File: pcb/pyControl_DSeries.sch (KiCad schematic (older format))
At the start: 14 parts, among them J1 Barrel_Jack, J2 RJ45-12PORT, U1 PyBoard-D-Series, U2 R-78E5.0-1.0, U3 TBD62083APG, U4 TBD62083APG, U5 TBD62083APG

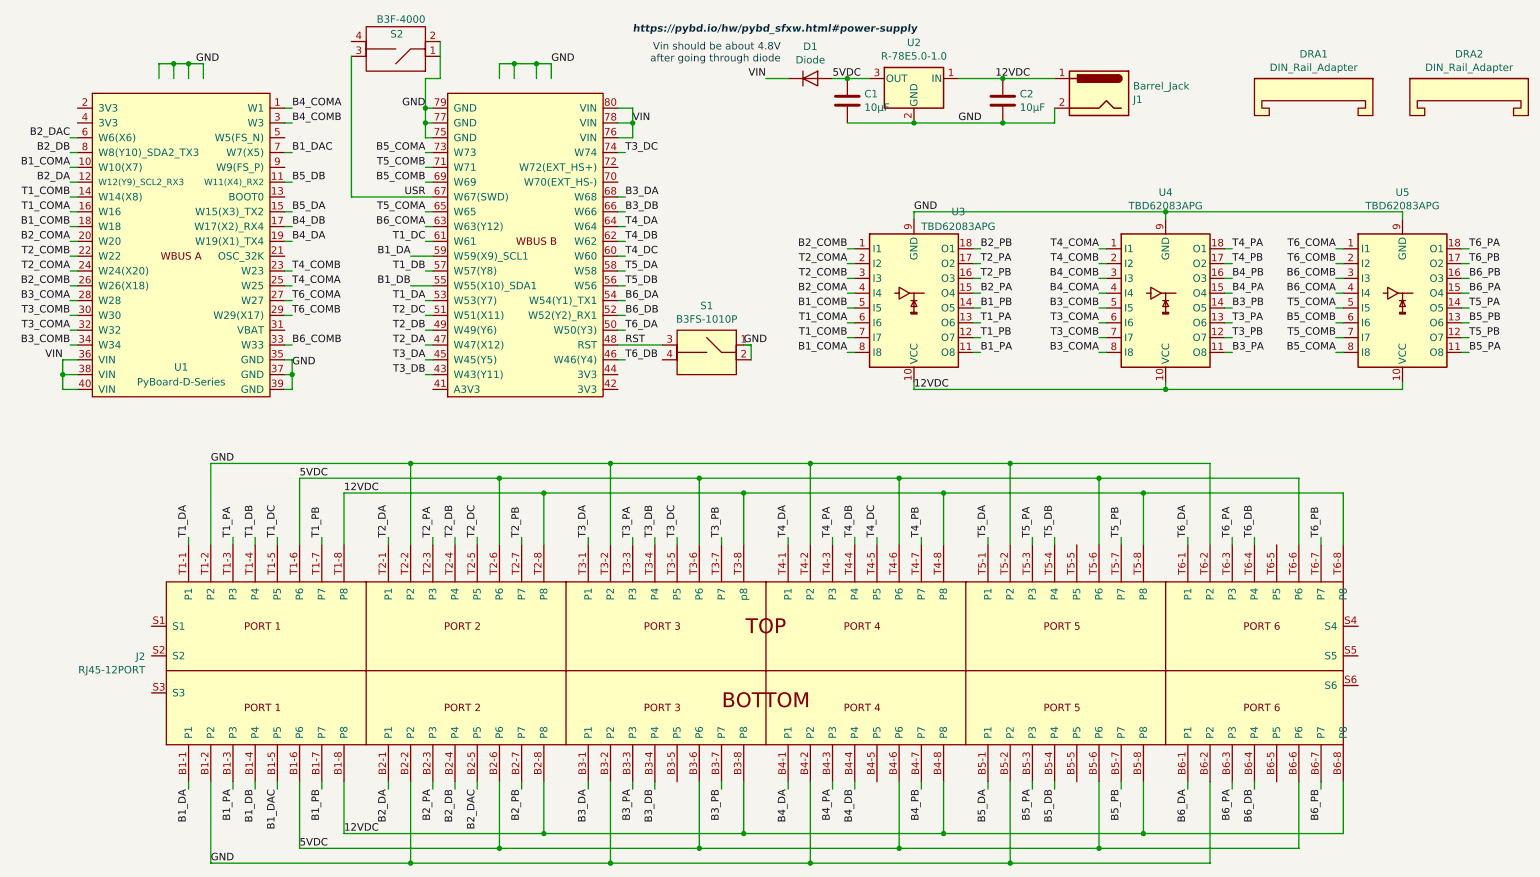
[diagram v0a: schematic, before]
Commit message: pcb version 1.3. W1 cannot be used as DIO, so now B4_COMA is connected to pin9 (W9). W69 cannot be used as DIO, so now B5_COMB is connected to pin5 (W5). Added microusb connector so that you can permanently plug into breakout board and talk to the pyboard via the Hirose connector. This enables usb communication with the pyboard while still allowing one to easily swap out pyboards if necessary. changed user switch to SMD part Shifted components around.
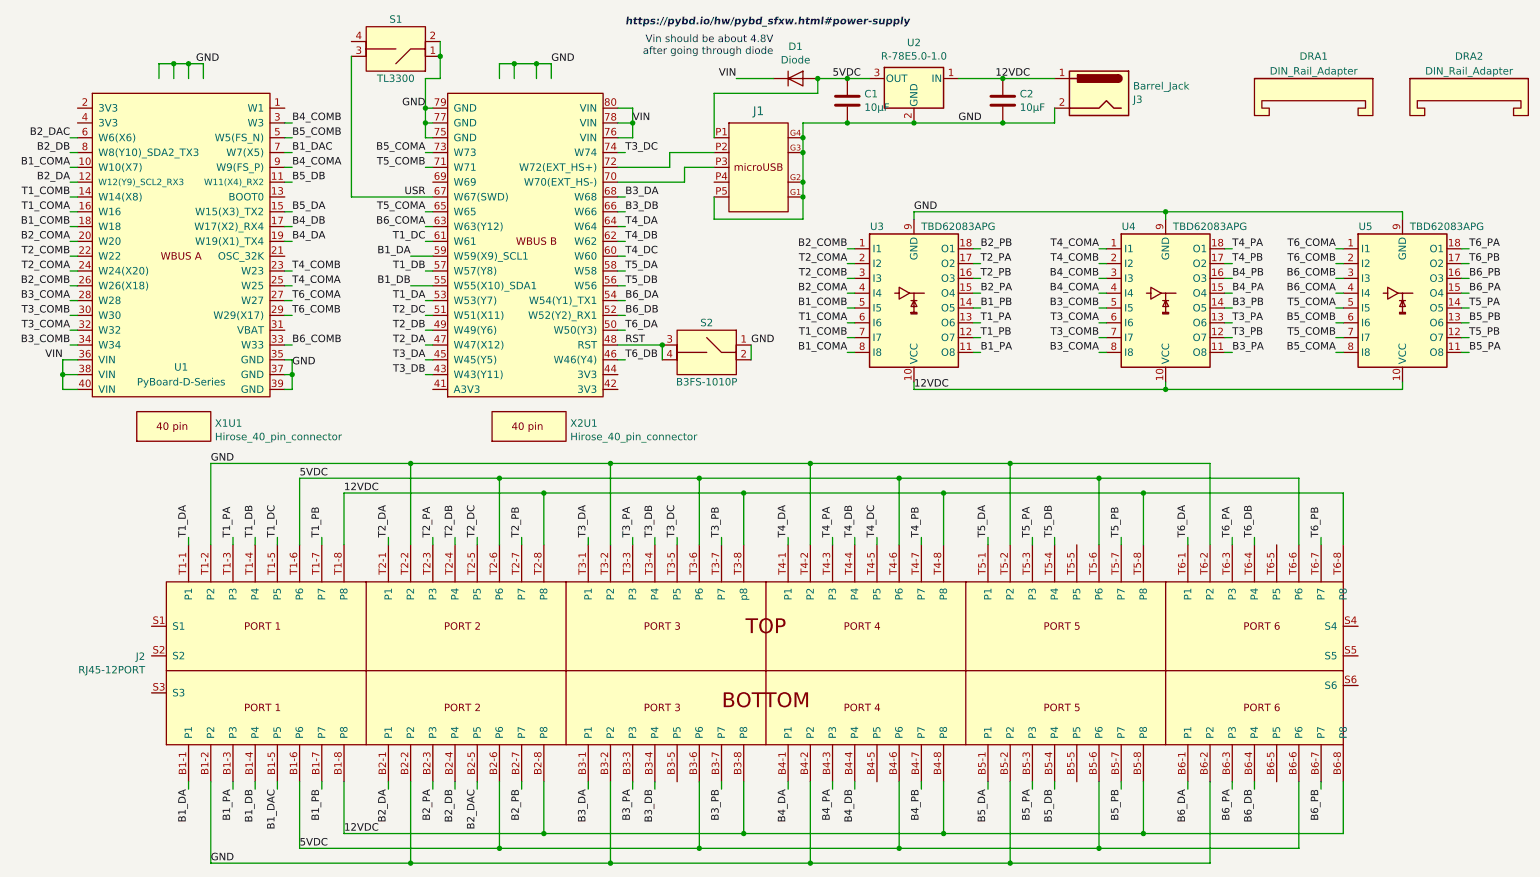
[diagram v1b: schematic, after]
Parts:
- removed S2: B3F-4000, asl_footprints:12mm_tactile_SPST, symbol asl_symbols:B3F-4000
- added J1: USB_micro_horz_socket_reinforced, asl_footprints:microUSB_horizontal_socket, symbol asl_symbols:USB_micro_horz_socket_reinforced
- added S1: TL3300, asl_footprints:12mm_tactile_smd, symbol asl_symbols:TL3300
- added X1U1, X2U1: Hirose_40_pin_connector, asl_footprints:Hirose_40_pin, symbol asl_symbols:Hirose_40_pin_connector
- renumbered J1 to J3, S1 to S2
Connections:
- net 5VDC: now also J1.P1
- net B4_COMA: now also U1.9 (W9(FS_P)); no longer U1.1 (W1)
- net B5_COMB: now also U1.5 (W5(FS_N)); no longer U1.69 (W69)
- net GND: now also J1.G1, J1.G2, J1.G3, J1.G4, J1.P5, S1.1 (in1), S1.2 (in2)
- net RST: now also S2.4 (out2)
- net USR: now also S1.3 (out1)
- net at U1.70 (W70(EXT_HS-)): now also J1.P3
- net at U1.72 (W72(EXT_HS+)): now also J1.P2
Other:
- moved on the sheet: D1

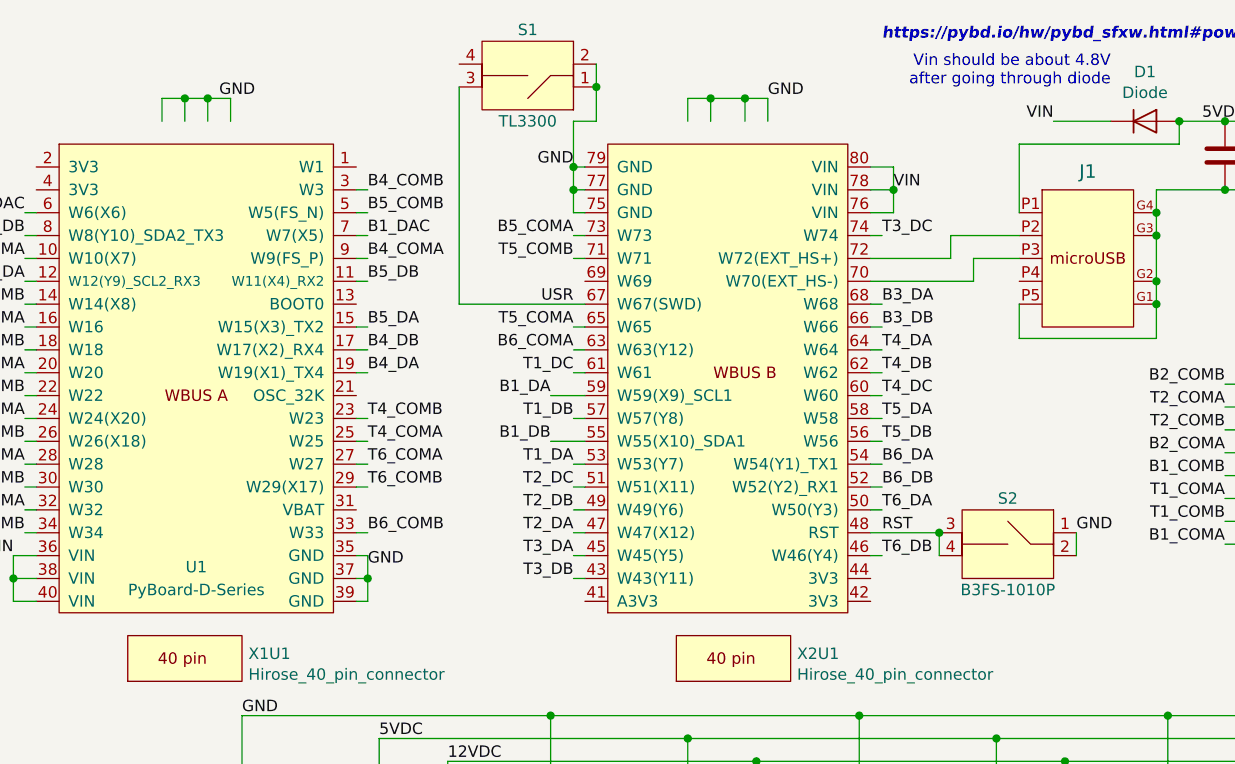
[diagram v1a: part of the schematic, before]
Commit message: PCB rev 1.4 removed mounting pads from D40 Hirose connector since that version of connector is discontinued. shifted pyboard connectors down and to the left so now an SD card can be inserted without interfering with microusb connector micro usb tx/rx were incorrectly wired. swapped buttons so user button is now closer to board edge (less likely to accidentally press reset on way to pressing user button).
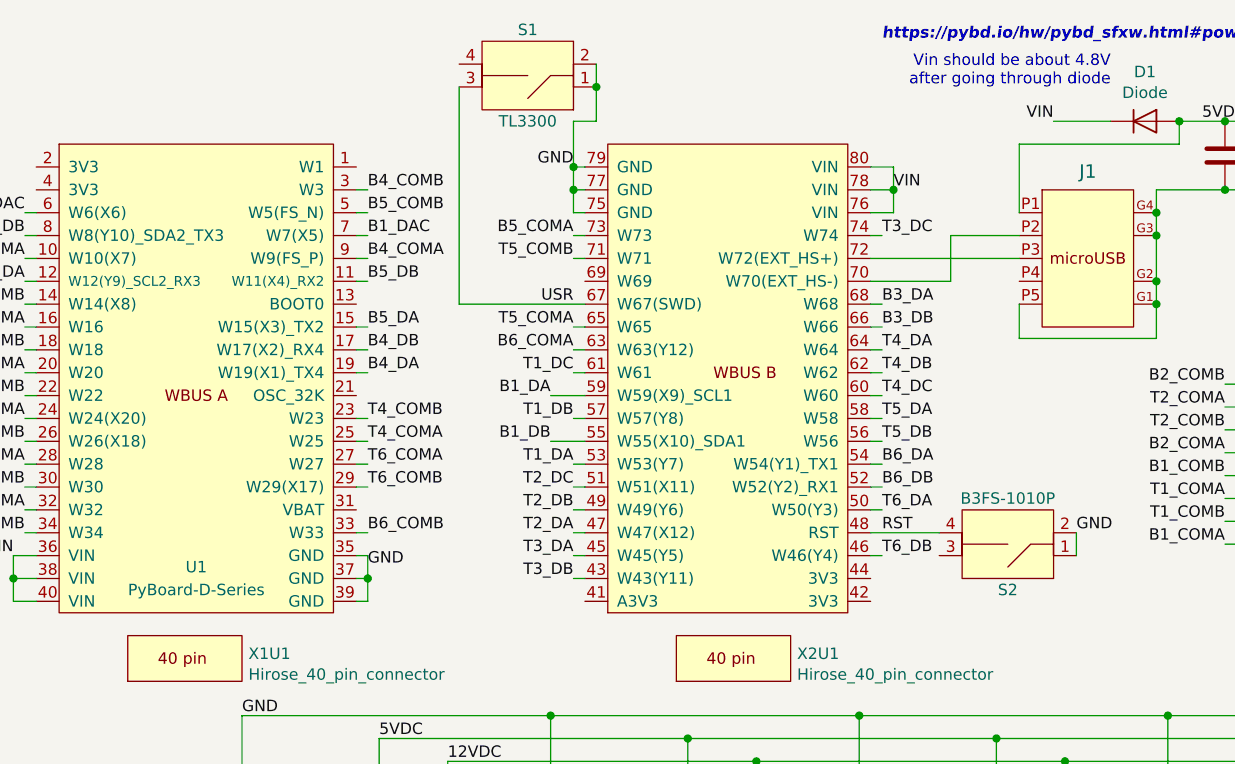
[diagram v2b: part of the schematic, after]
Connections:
- net RST: no longer S2.3 (out1)
- net at U1.70 (W70(EXT_HS-)): now also J1.P2; no longer J1.P3
- net at U1.72 (W72(EXT_HS+)): now also J1.P3; no longer J1.P2
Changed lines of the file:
@@
 Sheet 1 1
 Title "pyControl D-Series Breakout"
-Date "2019-07-26"
-Rev "1.3"
+Date "2019-08-05"
+Rev "1.4"
 Comp ""
 Comment1 ""
@@
 	1000 2850 1100 2850
 Connection ~ 1000 2950
-Wire Wire Line
-	1650 950  1650 850
-Wire Wire Line
-	1650 850  1750 850
 Text Label 1000 2850 2    50   ~ 0
 VIN
-Wire Wire Line
-	1750 850  1750 950
-Wire Wire Line
-	1750 850  1850 850
-Wire Wire Line
-	1850 850  1850 950
-Connection ~ 1750 850
-Wire Wire Line
-	1850 850  1950 850
-Wire Wire Line
-	1950 850  1950 950
-Connection ~ 1850 850
-Wire Wire Line
-	3950 850  4050 850
-Wire Wire Line
-	4050 850  4050 950
-Wire Wire Line
-	3950 850  3950 950
-Wire Wire Line
-	4200 950  4200 850
-Wire Wire Line
-	4200 850  4050 850
-Connection ~ 4050 850
-Wire Wire Line
-	4300 950  4300 850
-Wire Wire Line
-	4300 850  4200 850
-Connection ~ 4200 850
 Text Label 2550 2900 0    50   ~ 0
-GND
-Text Label 1900 850  0    50   ~ 0
-GND
-Text Label 4300 850  0    50   ~ 0
 GND
 Wire Wire Line
@@
 Wire Wire Line
 	2550 2750 2500 2750
-Wire Wire Line
-	4750 2750 5050 2750
 Wire Wire Line
 	8450 1850 8450 1900
@@
 	5400 1450 5100 1450
 Wire Wire Line
-	5100 1450 5100 1550
-Wire Wire Line
-	5100 1550 4750 1550
-Wire Wire Line
-	5400 1550 5200 1550
-Wire Wire Line
-	5200 1550 5200 1650
-Wire Wire Line
-	5200 1650 4750 1650
+	5400 1550 4750 1550
 $Comp
 L asl_symbols:Hirose_40_pin_connector X2U1
@@
 F 3 "https://omronfs.omron.com/en_US/ecb/products/pdf/en-b3f.pdf" H 5200 2700 50  0001 C CNN
 	1    5350 2800
-	-1   0    0    -1
-$EndComp
-Wire Wire Line
-	5050 2850 5050 2750
-Connection ~ 5050 2750
+	-1   0    0    1
+$EndComp
+Wire Wire Line
+	4750 2750 5050 2750
+Wire Wire Line
+	5100 1450 5100 1650
+Wire Wire Line
+	5100 1650 4750 1650
 $EndSCHEMATC

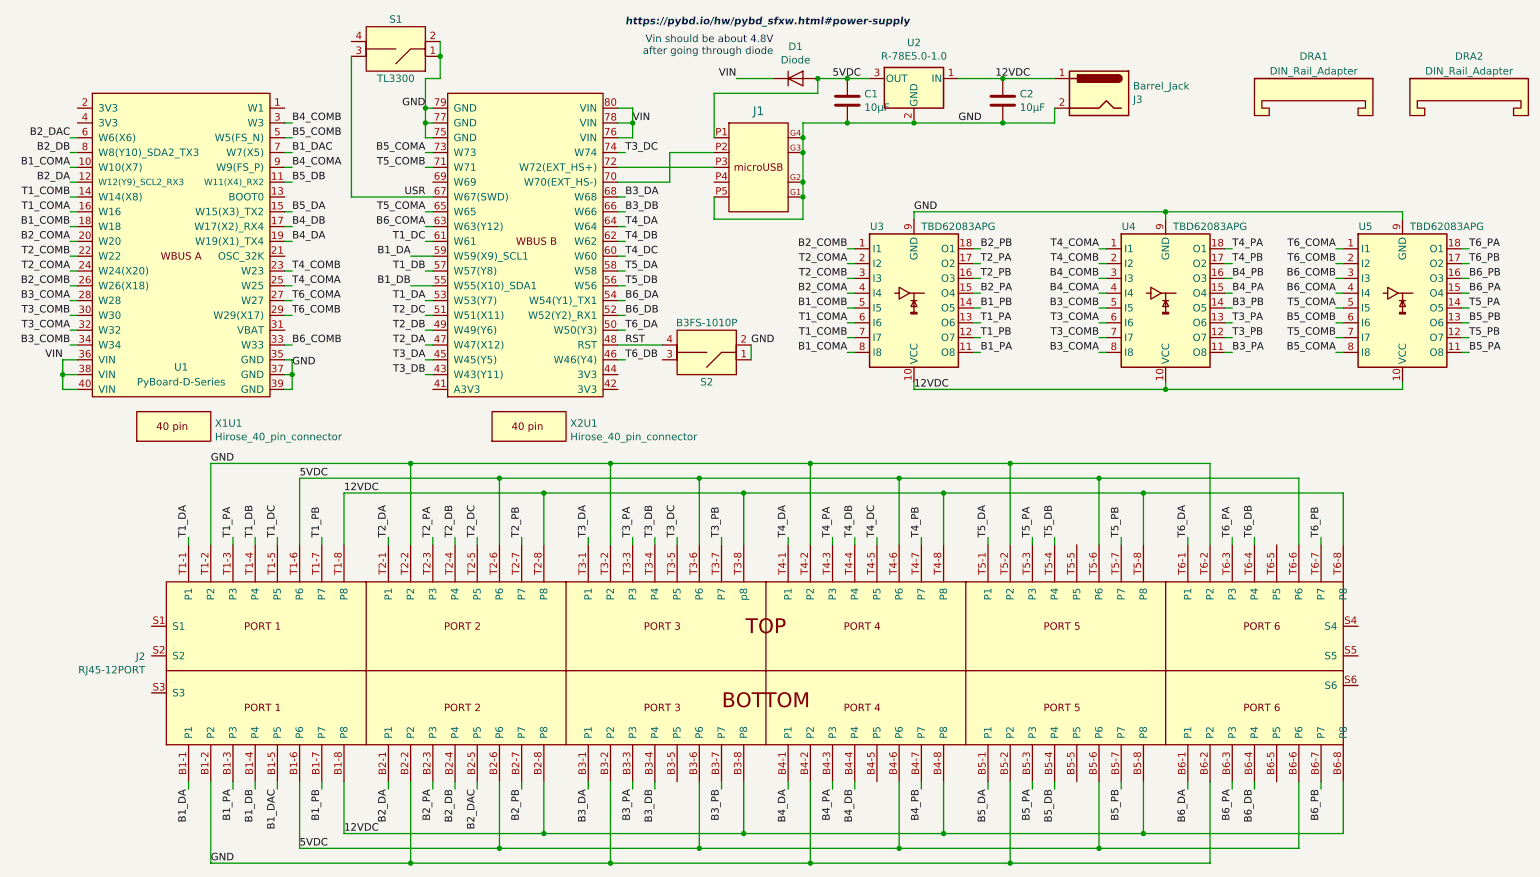
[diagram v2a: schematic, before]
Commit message: pcb v1.5. Rearranged pins to jack mapping.
To get top row inputs on separate interrupt vectors
T3_C was W74, now Q24
T4_B was W62, now W68
T4_C was W60, now W66
T6_A was W50, now W65
T6_A was W46, now W71

To maximize the number of analog inputs that are exposed
T4_A was W64, now W10
B3_A is now W63
B3_B is now W14

Design constraint priorities
All ports must have power 2 power pins and at least 2 DIO
DACs are grouped with I2c peripherals
All of peripherals are on bottom row
All if IO pins on top row are on separate external interrupt vectors. If you use the top ports for your digital inputs, you will never risk having conflicts of having already used an interrupt vector
15 Analog input pins are distributed through the DIO pins
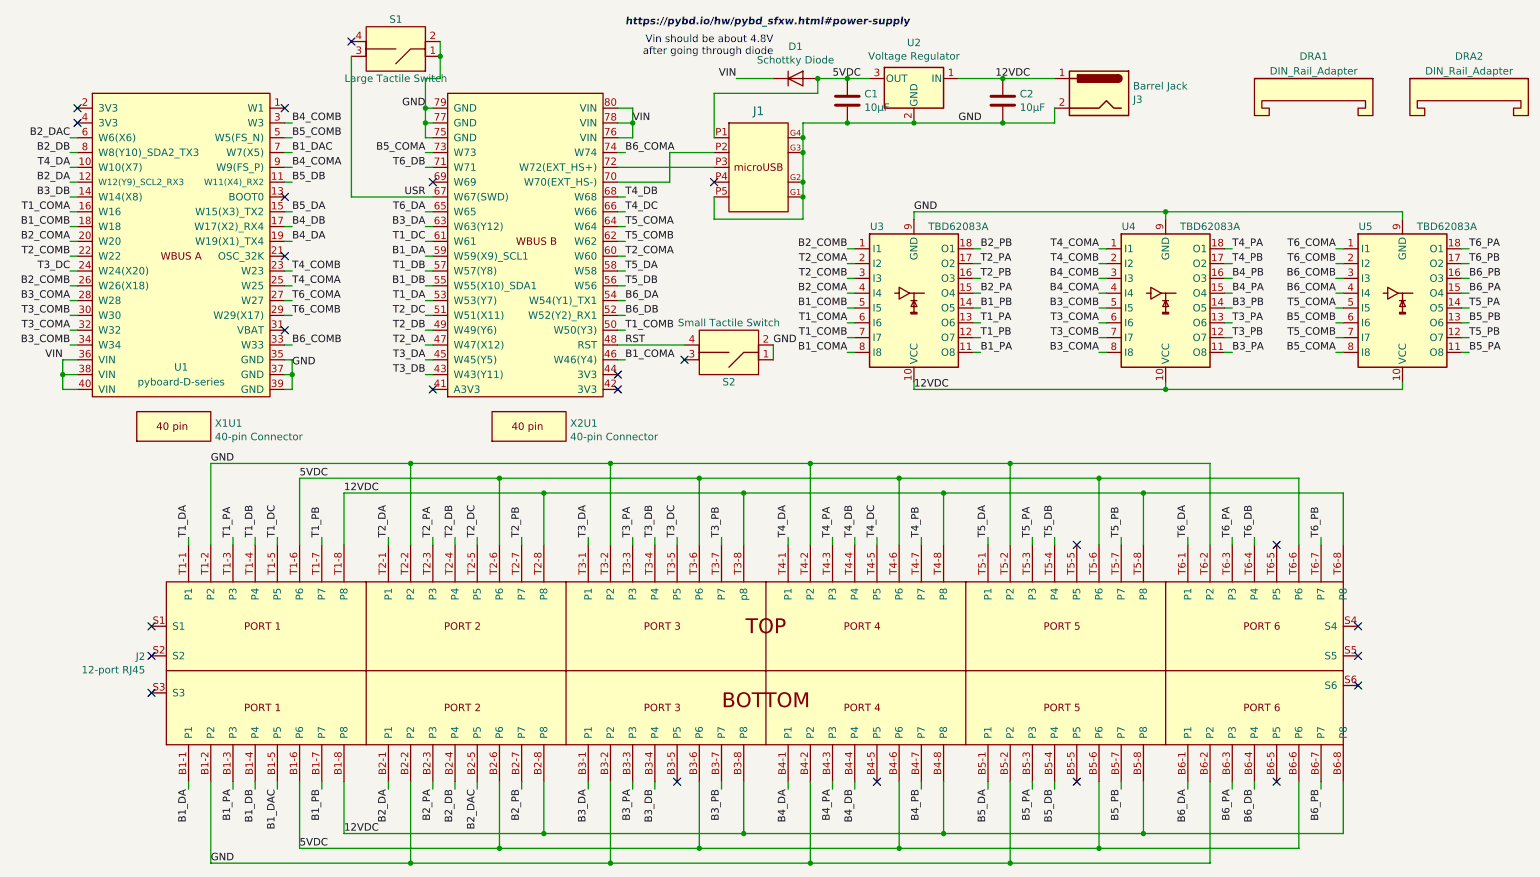
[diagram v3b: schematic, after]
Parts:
- D1: value Diode -> Schottky Diode
- DRA1, DRA2: DNP (none) -> 1
- J1: value USB_micro_horz_socket_reinforced -> MicroUSB Connector
- J2: value RJ45-12PORT -> 12-port RJ45
- J3: value Barrel_Jack -> Barrel Jack
- S1: value TL3300 -> Large Tactile Switch
- S2: value B3FS-1010P -> Small Tactile Switch
- U1: value PyBoard-D-Series -> pyboard-D-series; DNP (none) -> 1
- U2: value R-78E5.0-1.0 -> Voltage Regulator
- U3, U4, U5: value TBD62083APG -> TBD62083A
- X1U1, X2U1: value Hirose_40_pin_connector -> 40-pin Connector
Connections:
- net B1_COMA: now also U1.46 (W46(Y4)); no longer U1.10 (W10(X7))
- net B3_DA: now also U1.63 (W63(Y12)); no longer U1.68 (W68)
- net B3_DB: now also U1.14 (W14(X8)); no longer U1.66 (W66)
- net B6_COMA: now also U1.74 (W74); no longer U1.63 (W63(Y12))
- net T1_COMB: now also U1.50 (W50(Y3)); no longer U1.14 (W14(X8))
- net T2_COMA: now also U1.60 (W60); no longer U1.24 (W24(X20))
- net T3_DC: now also U1.24 (W24(X20)); no longer U1.74 (W74)
- net T4_DA: now also U1.10 (W10(X7)); no longer U1.64 (W64)
- net T4_DB: now also U1.68 (W68); no longer U1.62 (W62)
- net T4_DC: now also U1.66 (W66); no longer U1.60 (W60)
- net T5_COMA: now also U1.64 (W64); no longer U1.65 (W65)
- net T5_COMB: now also U1.62 (W62); no longer U1.71 (W71)
- net T6_DA: now also U1.65 (W65); no longer U1.50 (W50(Y3))
- net T6_DB: now also U1.71 (W71); no longer U1.46 (W46(Y4))
- no-connect marks 0 -> 25
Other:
- moved on the sheet: S2
